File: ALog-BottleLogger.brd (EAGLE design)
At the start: 120.7 x 44.5 mm, 103 parts, among them IC2 ATMEGA644M, Q1 220mA/50V/3.5Ω, Q11 220mA/50V/3.5Ω, Q12 4.3A/20V/54mΩ, Q5 4.3A/20V/54mΩ, Q6 4.3A/20V/54mΩ, Q7 4.3A/20V/54mΩ, Q8 220mA/50V/3.5Ω, Q9 220mA/50V/3.5Ω, U2 FT231X-Q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

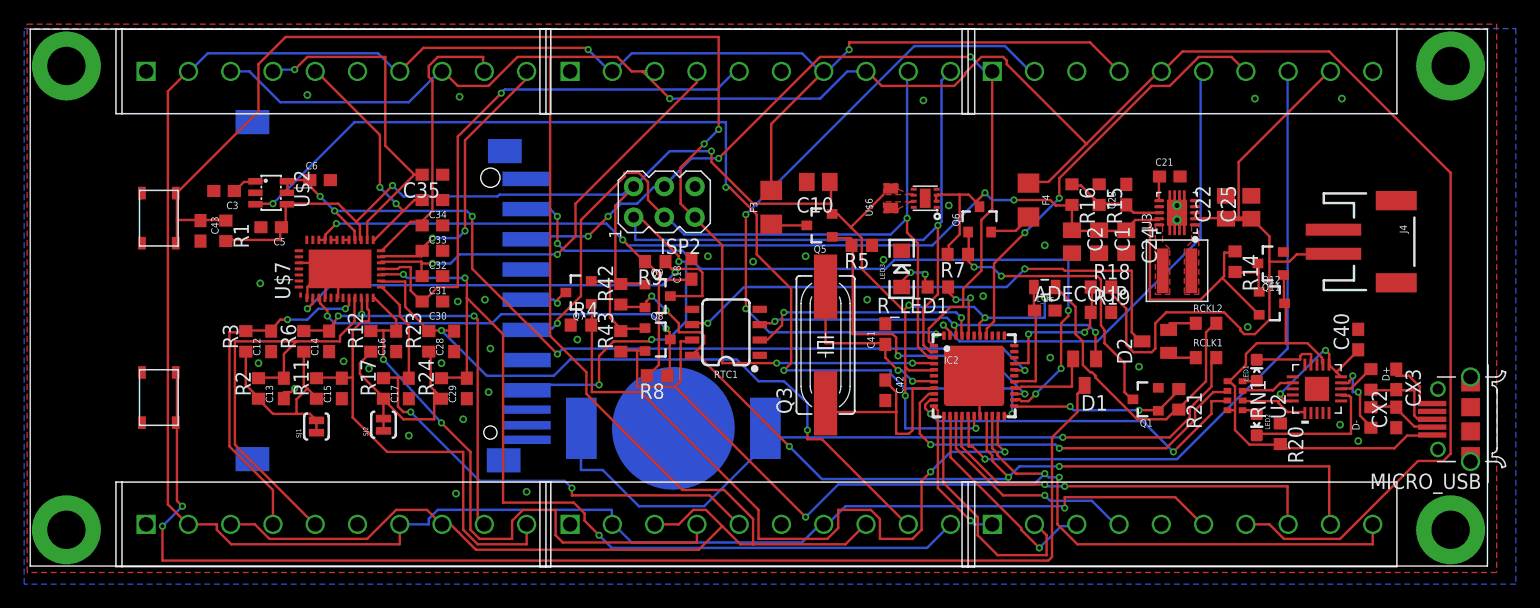
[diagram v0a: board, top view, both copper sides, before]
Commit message: Need to fix DTR connection and remove or isolate ground plane under crystal
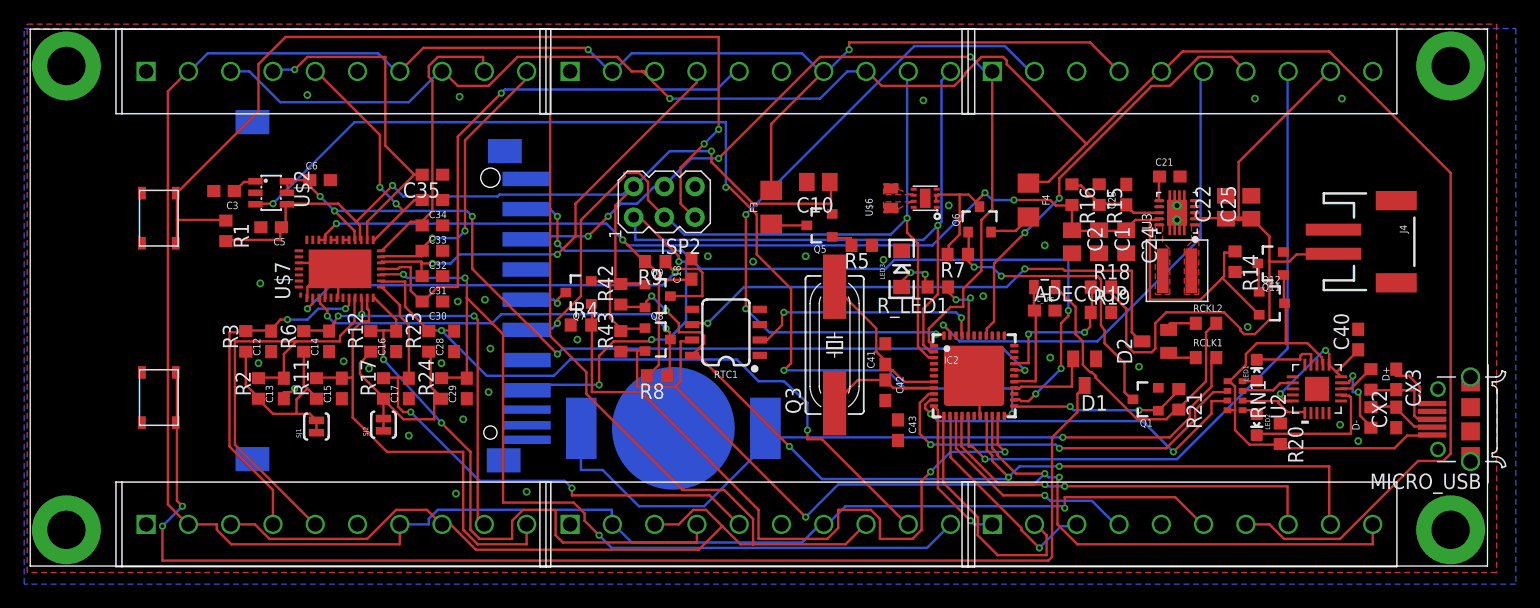
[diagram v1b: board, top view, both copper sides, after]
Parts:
- moved C43 60.1 mm to (71.8, 11.2)
- moved C41 1.65 mm to (70.8, 17.6)
- moved Q3 0.75 mm to (66.6, 18.3)
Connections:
- net DTR: now also C43.2
- net GND: no longer C43.2
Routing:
- net +3V3: track 161.3 -> 110.5 mm, vias 7 -> 2
- net RTC_INT: track 31.8 -> 0.00 mm, vias 3 -> 0
- net RST: track 108.2 -> 77.6 mm, vias 4 -> 2
- net 3.3V_EXT_CTRL: track 27.7 -> 2.26 mm, vias 2 -> 0
- net XTAL1: track 18.1 -> 9.29 mm
- net XTAL2: track 15.7 -> 12.8 mm, vias 2 -> 0
- net GND: vias 33 -> 32

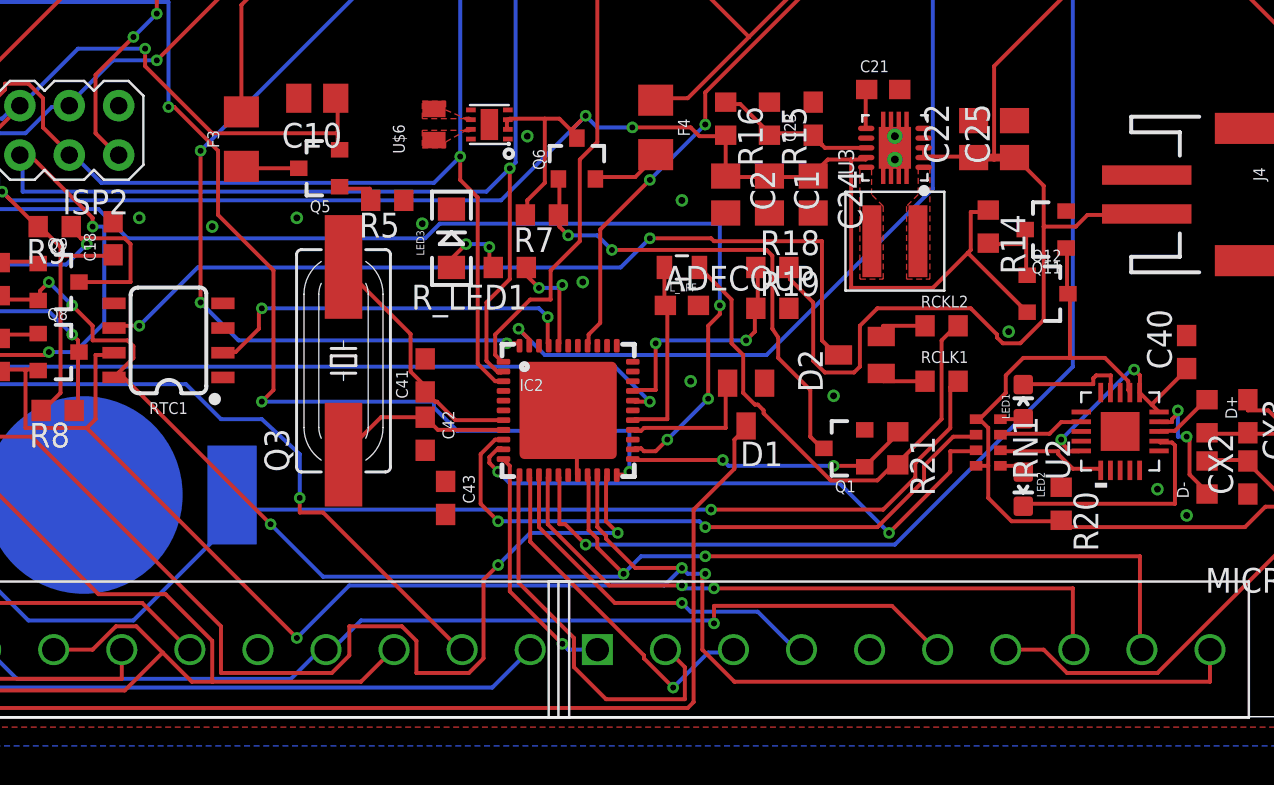
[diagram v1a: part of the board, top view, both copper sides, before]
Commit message: Routed DTR and removed fill planes from under crystal
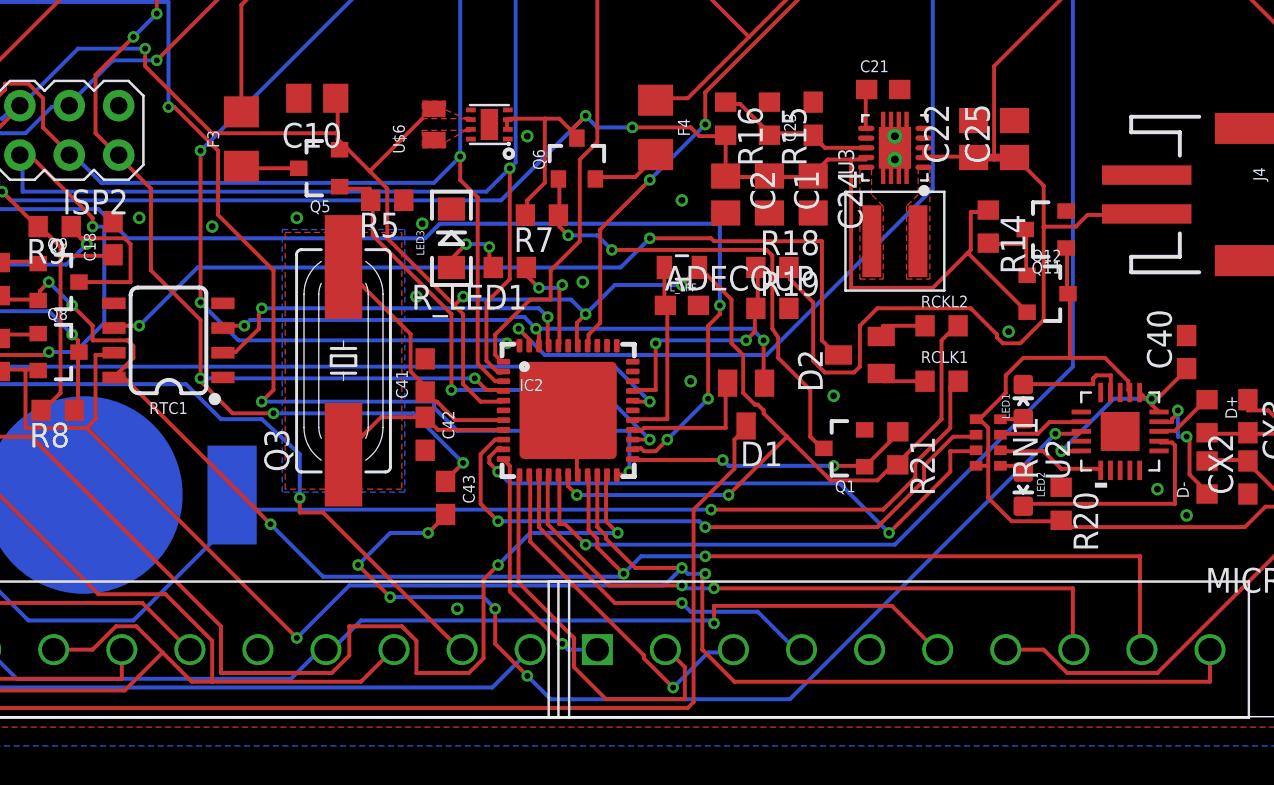
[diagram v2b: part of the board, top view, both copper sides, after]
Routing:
- net DTR: track 0.00 -> 52.4 mm, vias 0 -> 6
- net +3V3: track 110.5 -> 161.3 mm, vias 2 -> 7
- net RST: track 77.6 -> 123.4 mm, vias 2 -> 6
- net RTC_INT: track 0.00 -> 31.7 mm, vias 0 -> 3
- net 3.3V_EXT_CTRL: track 2.26 -> 25.9 mm, vias 0 -> 2
- net N$30: track 12.0 -> 11.0 mm
- net GND: vias 32 -> 34
- added copper zone on layer 16, net N$13
- added copper zone on layer 1, net N$9

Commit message: COM on ADC should be 2.5V divided from 5V not GND
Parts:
- R18: value 10k -> 953k
- R19: value 10k -> 143k
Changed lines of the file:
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@@
 </element>
 <element name="S1" library="Custom" package="SKRPABE010_(SWITCH)" value="SKRPABE010" x="10.65" y="13.95" rot="R270"/>
-<element name="R18" library="rcl" package="R0603@1" value="10k" x="88.65" y="23.1"/>
-<element name="R19" library="rcl" package="R0603@1" value="10k" x="88.65" y="21"/>
+<element name="R18" library="rcl" package="R0603@1" value="953k" x="88.65" y="23.1"/>
+<element name="R19" library="rcl" package="R0603@1" value="143k" x="88.65" y="21"/>
 <element name="U$2" library="bschulz" package="SOT23-6L" value="MAX6070" x="19.95" y="30.9" rot="R270"/>
 <element name="Q1" library="SparkFun-DiscreteSemi" package="SOT23-3" value="220mA/50V/3.5Ω" x="92.4" y="13.8" rot="R90">

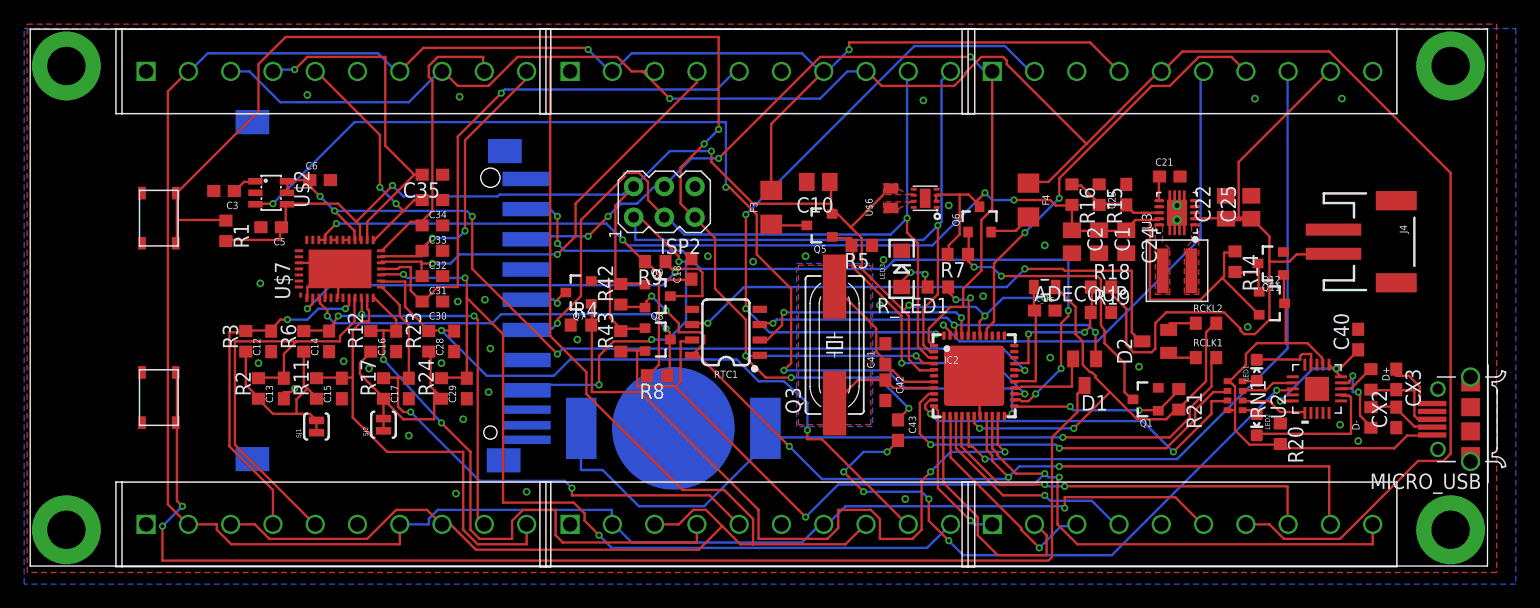
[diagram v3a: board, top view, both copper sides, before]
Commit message: improved 3V3 component layout
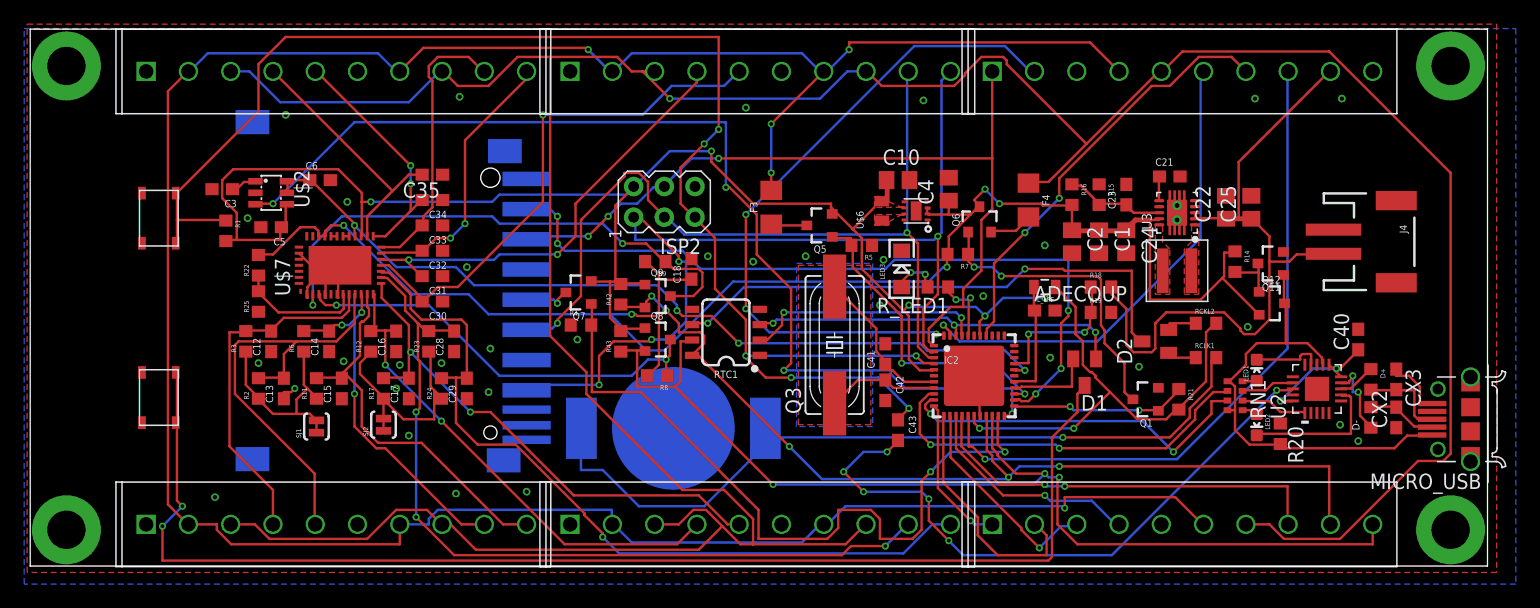
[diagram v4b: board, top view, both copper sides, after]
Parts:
- added C4: 10uF, rcl:C0805
- added R22, R25: 10k, rcl:R0603
- R1, R11, R12, R14, R17, R2, R20, R21, R23, R24, R3, R4, R42, R43, R5, R6, R7, R8, R9: device rcl:R0603@1 -> rcl:R0603
- R15, R19: value 143k -> 111k; device rcl:R0603@1 -> rcl:R0603
- R16, R18: value 953k -> 1M; device rcl:R0603@1 -> rcl:R0603
- moved C10 6.60 mm to (71.8, 31.9), turned to 0 degrees
- moved U$3 1.29 mm to (73.3, 29.4)
- moved U$6 1.29 mm to (70.5, 29.4)
- moved U$7 0.30 mm to (25.6, 24.9)
- moved C3 0.21 mm to (15.9, 31.2)
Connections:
- new net N$16: R22.1, R25.2, U$7.7
- net +5V: now also C4.1, R22.2
- net GND: now also C4.2, R25.1; no longer U$7.7
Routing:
- net +5V: track 124.6 -> 136.2 mm, vias 4 -> 5
- net ADC6: track 57.2 -> 68.0 mm, vias 2 -> 3
- net N$16: track 0.00 -> 10.5 mm
- net +3V3: track 161.3 -> 171.8 mm
- net ADC4: track 49.9 -> 40.9 mm
- net ADC7: track 75.6 -> 66.6 mm, vias 3 -> 1
- net ADC13: track 28.2 -> 21.6 mm, vias 1 -> 0
- net ADC3: track 38.5 -> 32.8 mm
- net 1.8V_REF: track 76.0 -> 70.9 mm, vias 5 -> 4
- net ADC8: track 47.2 -> 43.2 mm
- net ADC2: track 34.1 -> 30.0 mm
- net MOSI/D5: track 71.1 -> 67.2 mm, vias 4 -> 3
- net SCL_HV: track 41.3 -> 45.2 mm
- net SDA: track 91.5 -> 89.3 mm
- net GND: track 23.8 -> 25.8 mm
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
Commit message: Final revisions made, many changes, 5V external mosphet update, RTC power configuration, add 5V psync control pin, change external power control pins, add barrel jack, rerouted whole board
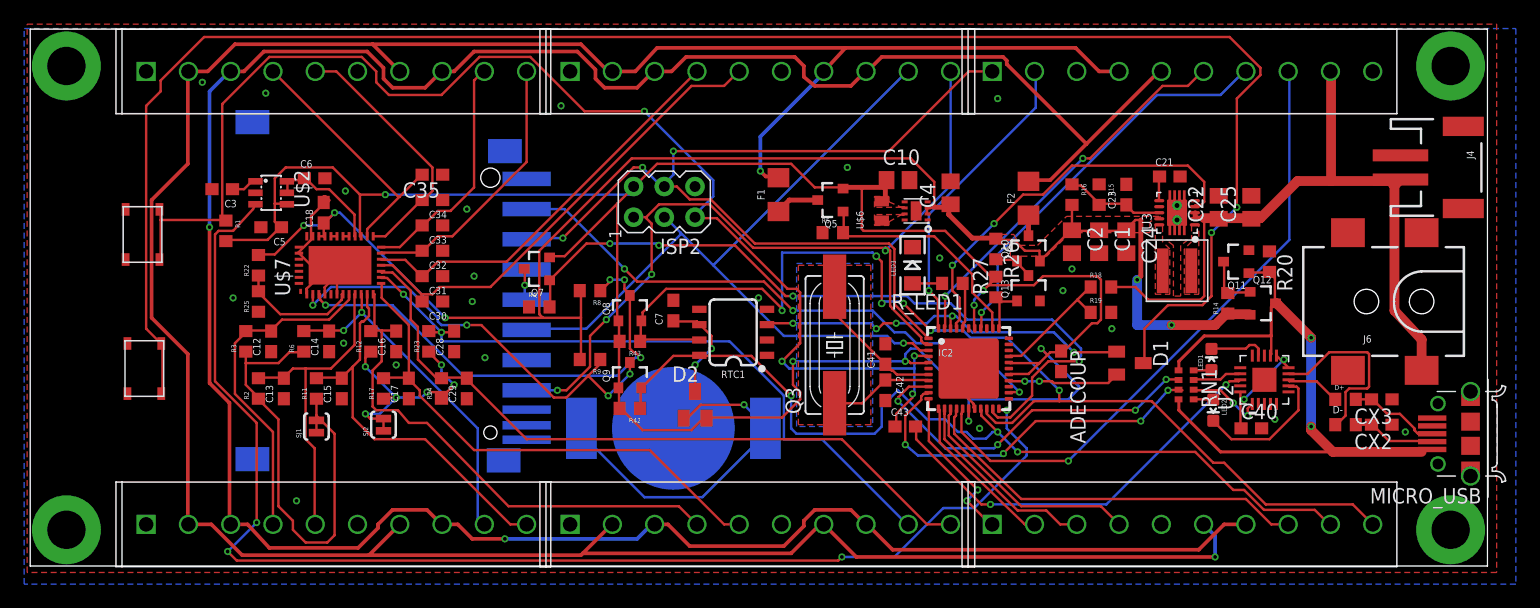
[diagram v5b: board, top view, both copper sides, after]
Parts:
- removed F3, F4: 6V/0.5A, SparkFun-Fuses:1206
- removed L_LPF: 10uH, SparkFun:0805
- removed Q1: 220mA/50V/3.5Ω, SparkFun-DiscreteSemi:SOT23-3
- removed Q6: 4.3A/20V/54mΩ, SparkFun-DiscreteSemi:SOT23-3
- removed R21, R7: 10k, rcl:R0603
- removed RCKL2, RCLK1: 220, rcl:R0603
- added C7: 0.1uF, rcl:C0603
- added F1, F2: PPTC_HALF-AMP, bschulz:1206
- added J6: 5.5x2.1mm Barrel, bschulz:POWER_JACK_SMD
- added Q10: MOSFET_PCH-IRLML2244, bschulz:SOT23-3
- added Q13: MOSFET-NCH-BSS138, bschulz:SOT23-3
- added R26: 10k, bschulz:R0603
- added R27: (no value), bschulz:R0603
- moved D2 38.5 mm to (55.0, 13.3), turned to 0 degrees
- moved C18 30.8 mm to (24.3, 29.2)
- moved R20 14.3 mm to (102.6, 25.2)
- moved C40 11.5 mm to (101.1, 11.4), turned to 0 degrees
- moved R9 9.73 mm to (46.4, 17.1)
- moved R42 9.48 mm to (49.6, 13.1), turned to 180 degrees
- moved R8 8.97 mm to (46.4, 22.8)
- moved J4 8.28 mm to (117.2, 33.0)
- moved Q9 6.97 mm to (49.6, 15.8), turned to 0 degrees
- moved U2 4.41 mm to (102.2, 15.4)
- moved ADECOUP 4.41 mm to (85.3, 16.9), turned to 270 degrees
- moved RN1 4.15 mm to (95.7, 15.0)
- moved Q7 3.96 mm to (42.0, 24.6)
- moved LED1 3.86 mm to (97.8, 17.1)
- moved D1 3.82 mm to (91.0, 16.8), turned to 270 degrees
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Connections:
- removed net AVCC: ADECOUP.1, IC2.27, L_LPF.2
- removed net MCU_ADC2: IC2.35
- removed net MCU_ADC3: IC2.34
- removed net N$14: F4.2, Q6.2
- removed net N$31: D2.2, RCKL2.1
- removed net N$38: D2.1, RCLK1.1
- removed net RTC_BATT: CLOCK_BATT.POWER0, CLOCK_BATT.POWER1, RCLK1.2
- removed net RTC_EN: IC2.41, RTC1.2
- new net D20: IC2.23
- new net D22: IC2.25
- new net N$20: F2.1, Q10.3
- new net N$23: Q10.1, Q13.3, R26.2
- new net PSYNC: IC2.41, U3.4
- net +3V3: now also ADECOUP.1, D2.2, IC2.27, IC2.29, R27.2; no longer L_LPF.1, R21.2, RCKL2.2
- net +5V: now also Q10.2, R26.1; no longer Q6.3, R7.2
- net 1.8V_REF: no longer IC2.29
- net 3.3V_EXT_CTRL: now also IC2.35; no longer IC2.25
- net 5V_EXT_CTRL: now also IC2.34, Q13.1, R27.1; no longer IC2.23, Q1.1, R21.1
- net BATT+: now also J6.VIN0
- net EXT_3.3V: now also F1.2; no longer F3.2
- net EXT_5V: now also F2.2; no longer F4.1
- net GND: now also C7.2, J6.GND, J6.P$4, Q13.2, RTC1.2; no longer Q1.2
- net N$17: now also F1.1; no longer F3.1
- net N$37: now also C7.1
- net N$6: now also CLOCK_BATT.POWER0, CLOCK_BATT.POWER1, D2.1; no longer Q1.3, Q6.1, R7.1
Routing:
- net RTC_BATT: track 67.0 -> 0.00 mm, vias 1 -> 0
- net 1.8V_REF: track 70.9 -> 10.3 mm, vias 4 -> 0
- net EXT_5V: track 283.4 -> 229.2 mm, vias 1 -> 2
- net N$39: track 105.7 -> 150.8 mm
- net N$37: track 44.6 -> 8.88 mm
- net PSYNC: track 0.00 -> 33.1 mm, vias 0 -> 2
- net SS/D4: track 55.7 -> 25.4 mm, vias 3 -> 1
- net +3V3: track 171.8 -> 201.1 mm
- net N$24: track 16.7 -> 38.0 mm
- net 1.8V_EN: track 87.5 -> 108.4 mm
- net RTC_EN: track 19.8 -> 0.00 mm, vias 2 -> 0
- net DTR: track 52.4 -> 34.4 mm, vias 6 -> 2
- net VUSB: track 38.9 -> 56.0 mm, vias 0 -> 2
- net SD_CS: track 62.8 -> 48.0 mm, vias 5 -> 3
- net RST: track 123.4 -> 109.6 mm, vias 6 -> 4
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- added copper zone on layer 1, net +5V
- added copper zone on layer 1, net N$15

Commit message: Straightened wires, very minor edits
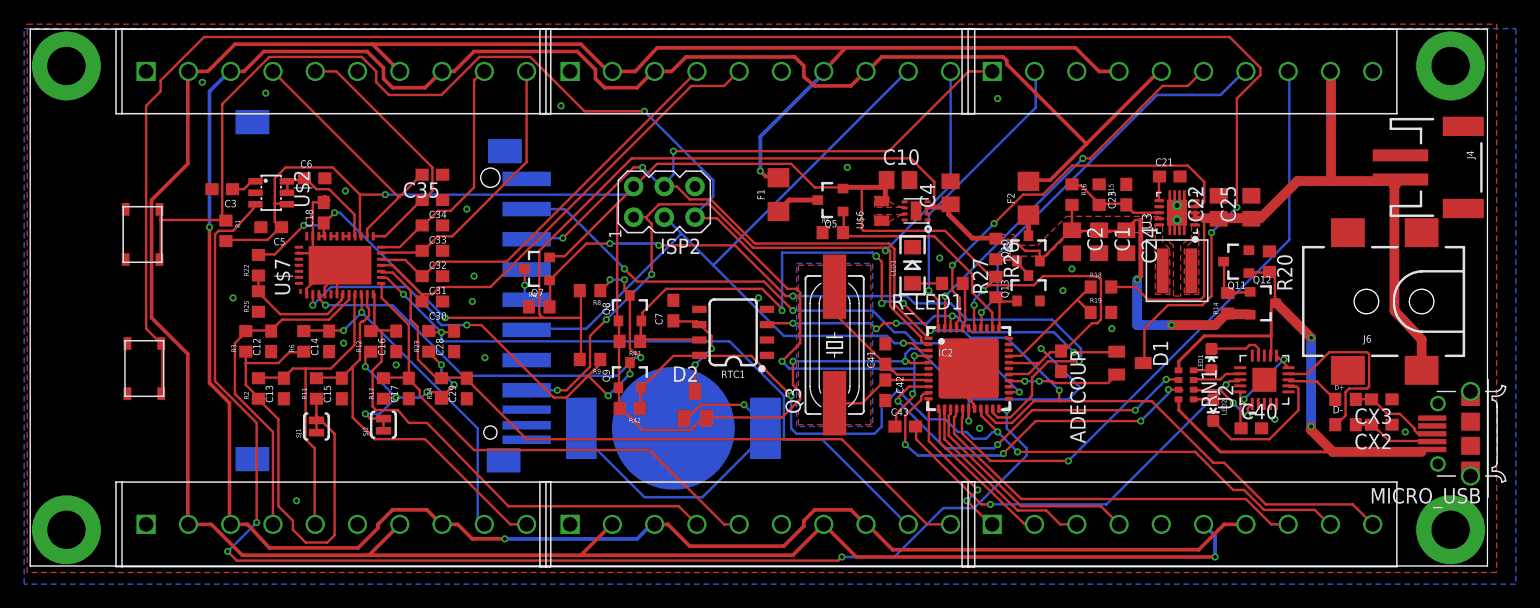
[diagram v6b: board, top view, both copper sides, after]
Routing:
- net GND: track 23.7 -> 27.5 mm
